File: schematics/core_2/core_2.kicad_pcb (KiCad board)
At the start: 2 copper layers, 100 x 91.1 mm, 24 parts, among them U1 74LS04, U2 74LS574, U3 74LS02, U5 74LS00

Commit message: silklayer check
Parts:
- moved kibuzzard-6911C9E9 1.10 mm to (193.5, 26.5)

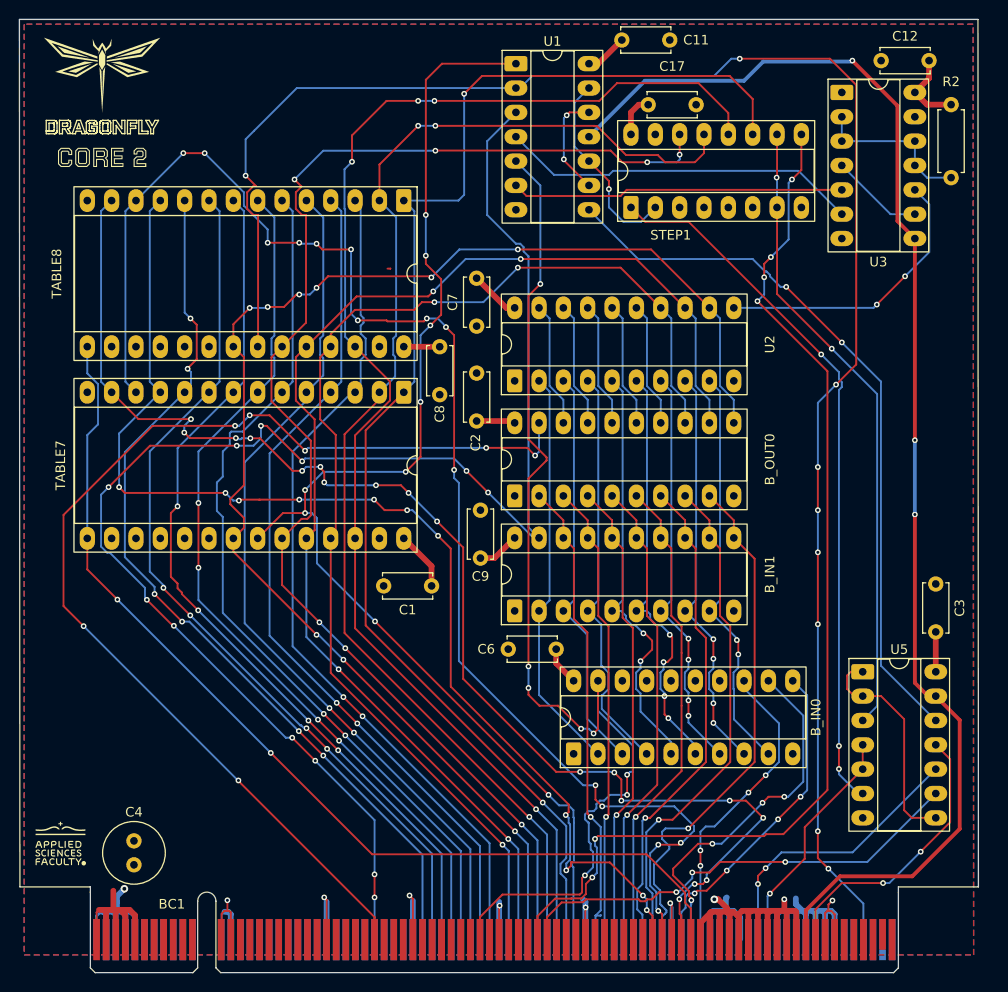
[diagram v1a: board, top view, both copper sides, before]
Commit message: fix(core2): changed vcc and gnd connection  + cooper clearence
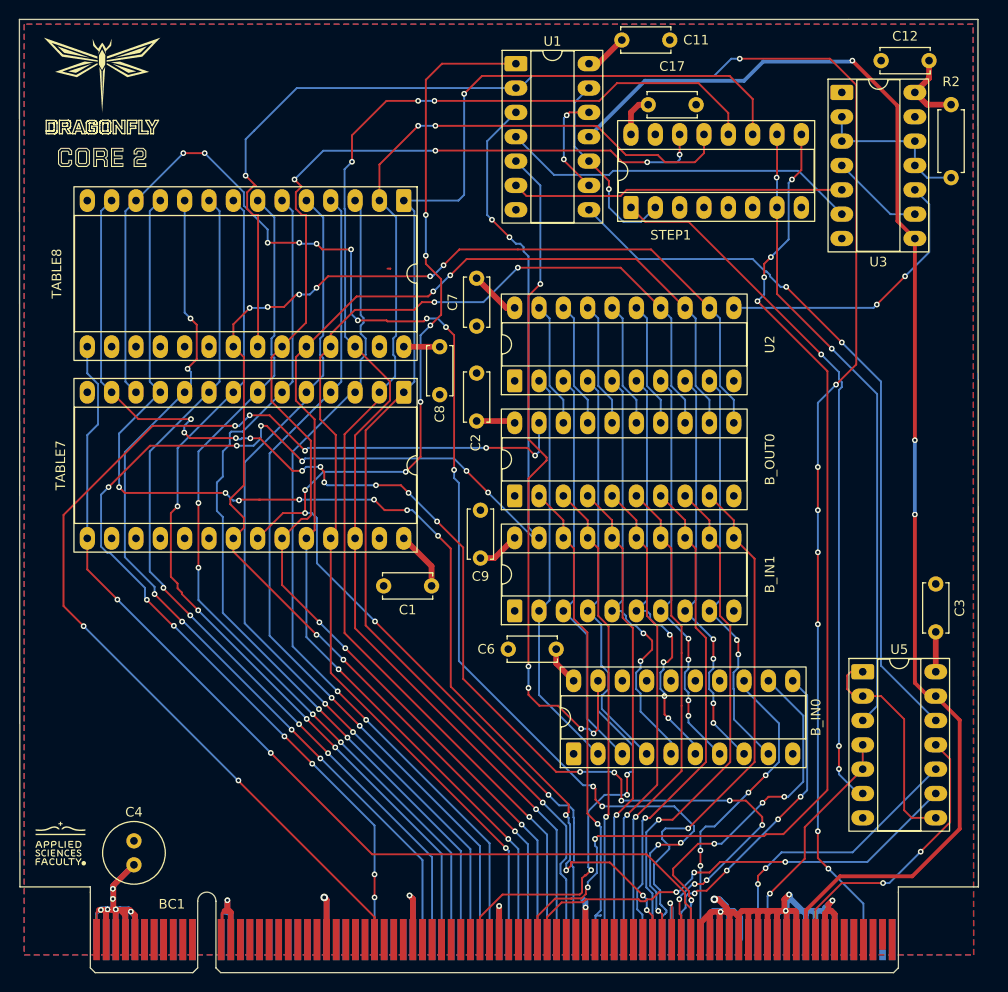
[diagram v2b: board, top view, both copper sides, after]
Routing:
- net GND: track 152.6 -> 160.5 mm, vias 9 -> 11
- net VCC: track 92.0 -> 99.6 mm, vias 1 -> 6
- net /~{UPDATE_FR}: track 115.4 -> 114.7 mm
- net /~{LOAD_FR}: track 161.5 -> 161.2 mm, vias 12 -> 14

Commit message: fix(alu, core2, interface): vcc conection some routing issues
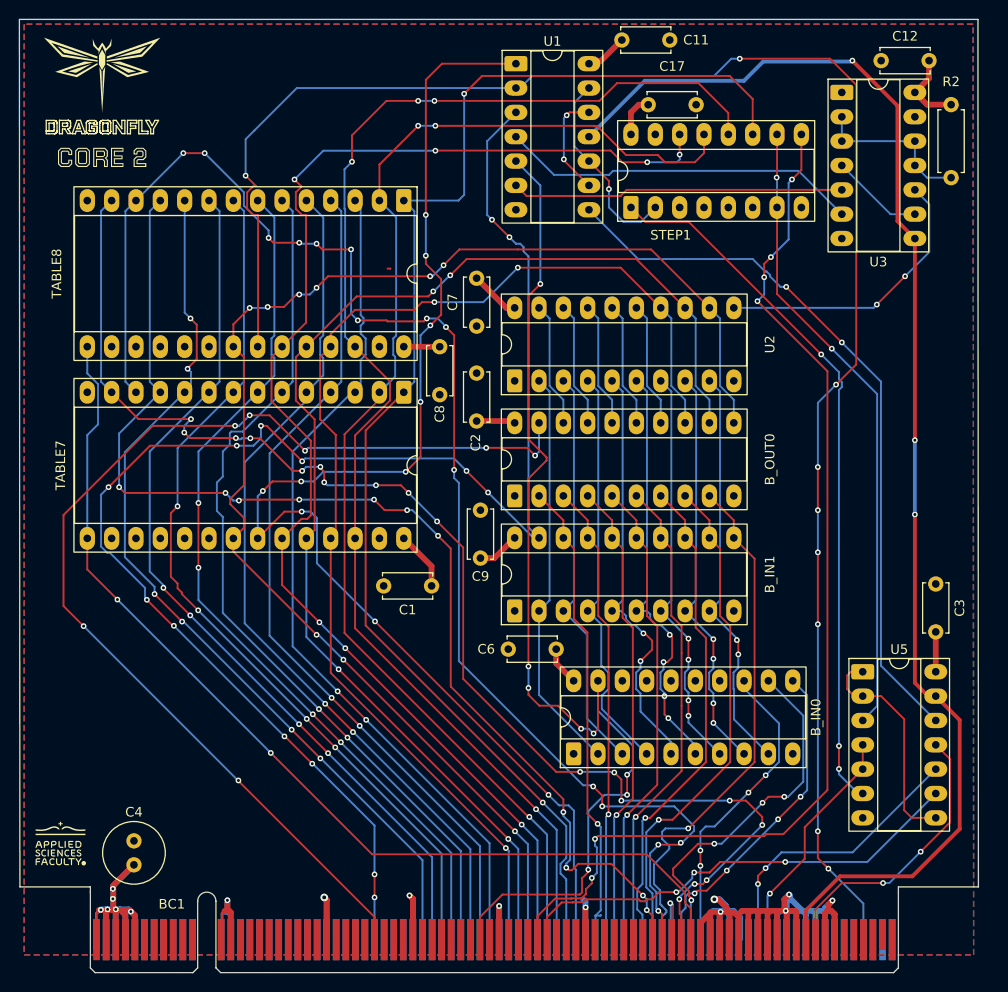
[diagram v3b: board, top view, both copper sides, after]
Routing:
- net /STATE15: track 130.3 -> 137.8 mm, vias 9 -> 10
- net /IntEnable: track 124.1 -> 123.3 mm
- net GND: track 160.5 -> 161.1 mm

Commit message: fix: removed in control pins daisy chains
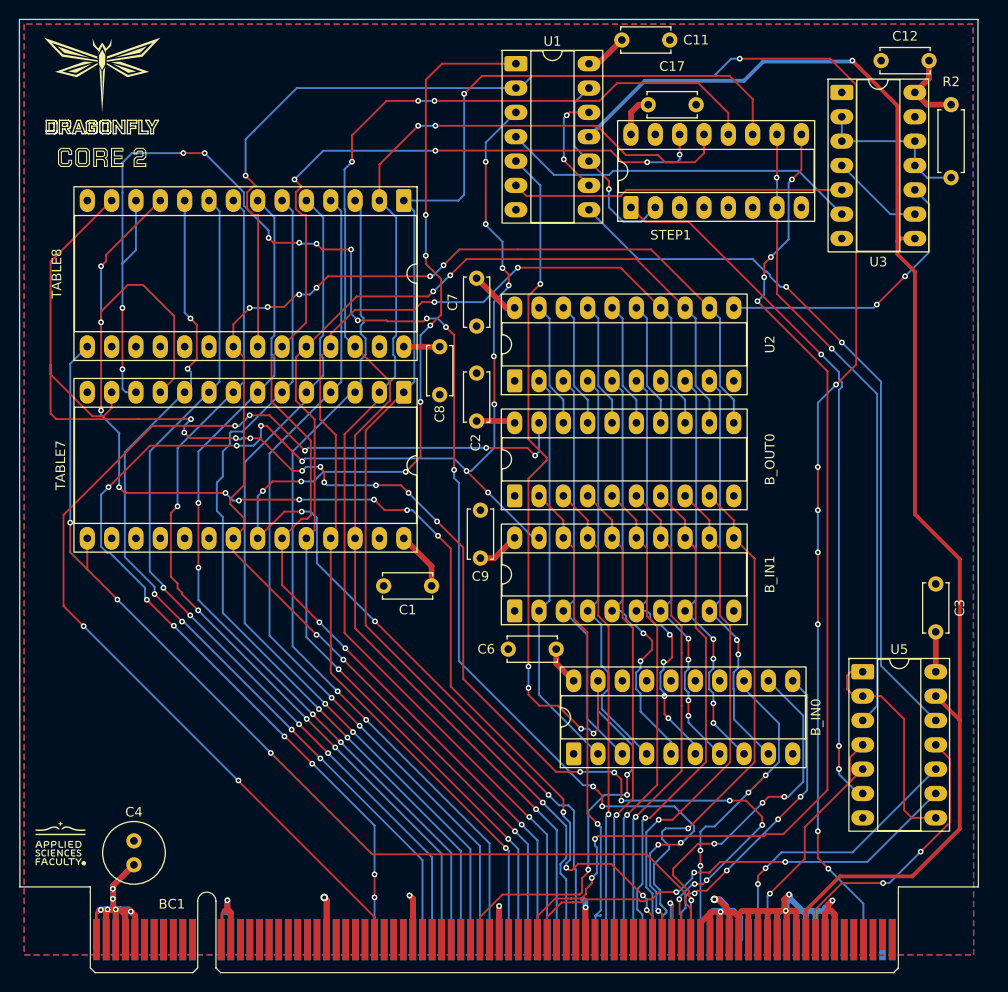
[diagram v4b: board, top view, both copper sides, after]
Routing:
- net /AddrDecrement: track 136.7 -> 157.3 mm
- net /IntEnable: track 123.3 -> 143.8 mm, vias 11 -> 14
- net /~{IntDisable}: track 151.8 -> 162.9 mm, vias 15 -> 17
- net /~{LOAD_FR}: track 161.2 -> 154.9 mm, vias 14 -> 18
- net /~CLK: track 138.6 -> 144.5 mm, vias 3 -> 1
- net /AddrIncrement: track 105.6 -> 109.4 mm, vias 2 -> 3
- net /Reset: track 24.4 -> 26.3 mm

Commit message: fix(alu, core_1_2, interface): put vcc zones on back layer
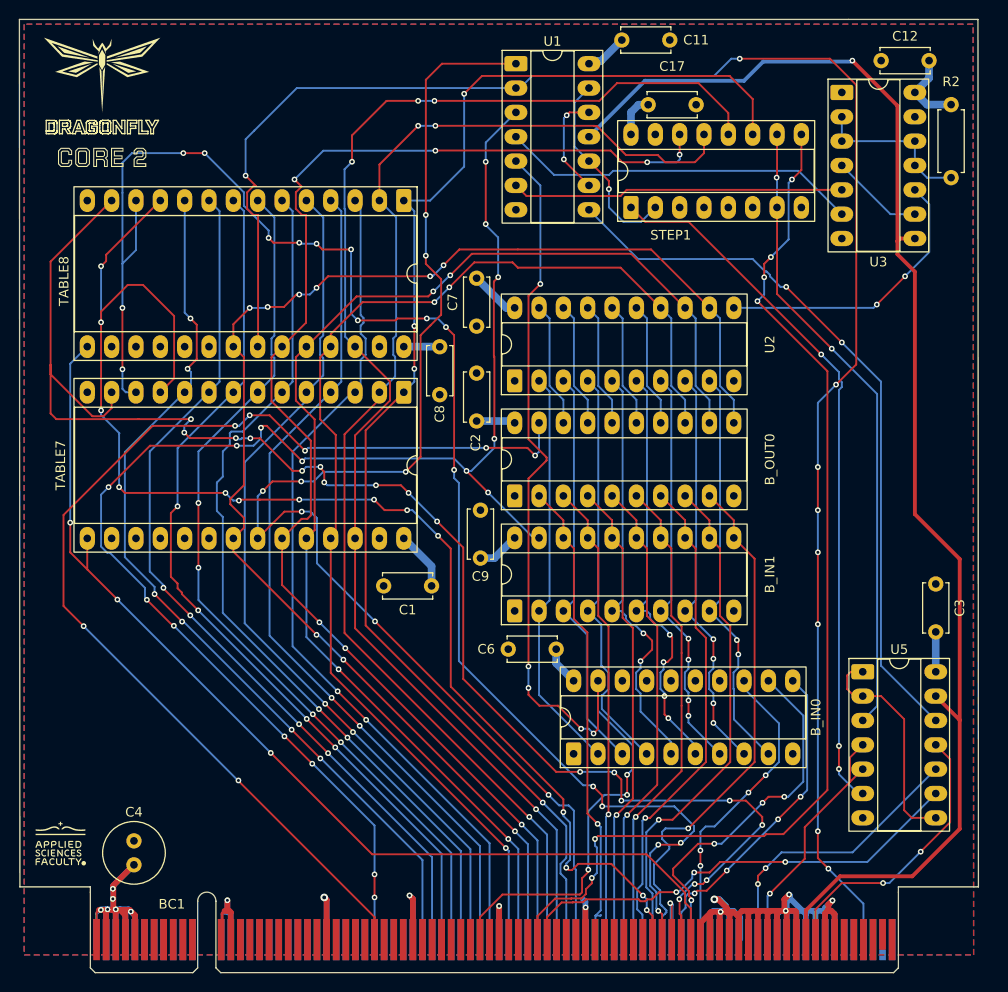
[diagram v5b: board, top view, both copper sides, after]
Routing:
- net /STATE14: track 141.5 -> 139.8 mm, vias 2 -> 4
- net /~{LOAD_FR}: track 154.9 -> 153.9 mm, vias 18 -> 16
- net /STATE15: vias 10 -> 8

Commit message: added testpoints on core 2
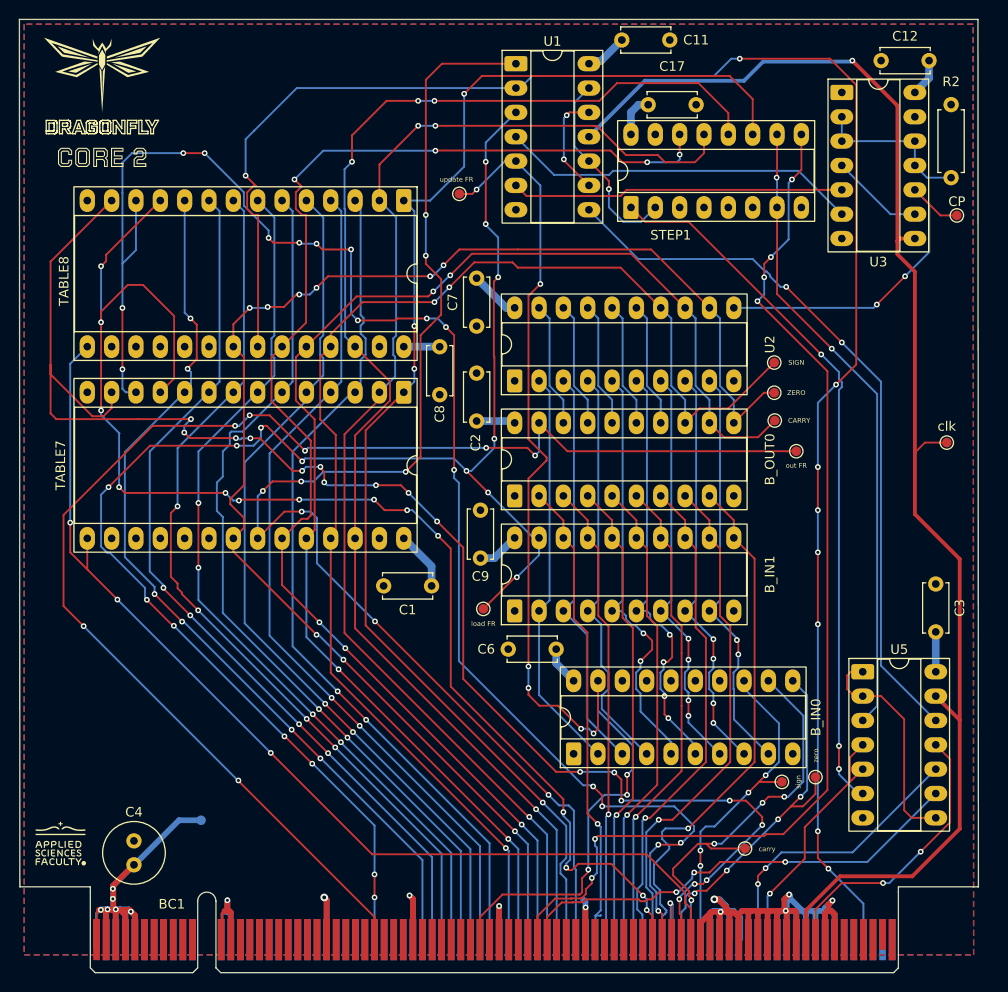
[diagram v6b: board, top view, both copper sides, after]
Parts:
- added CARRY: TestPoint, TestPoint:TestPoint_Pad_D1.0mm, F.Cu at (263.7, 54.0)
- added CP: TestPoint, TestPoint:TestPoint_Pad_D1.0mm, F.Cu at (282.7, 32.5)
- added SIGN: TestPoint, TestPoint:TestPoint_Pad_D1.0mm, F.Cu at (263.6, 47.9)
- added TP1: TestPoint, TestPoint:TestPoint_Pad_D1.0mm, B.Cu at (203.8, 95.7)
- added ZERO: TestPoint, TestPoint:TestPoint_Pad_D1.0mm, F.Cu at (263.6, 51.0)
- added carry: TestPoint, TestPoint:TestPoint_Pad_D1.0mm, F.Cu at (260.6, 98.6)
- added clk: TestPoint, TestPoint:TestPoint_Pad_D1.0mm, F.Cu at (281.6, 56.2)
- added load FR: TestPoint, TestPoint:TestPoint_Pad_D1.0mm, F.Cu at (233.3, 73.6)
- added out FR: TestPoint, TestPoint:TestPoint_Pad_D1.0mm, F.Cu at (265.9, 57.1)
- added sign: TestPoint, TestPoint:TestPoint_Pad_D1.0mm, F.Cu at (264.4, 91.7)
- added update FR: TestPoint, TestPoint:TestPoint_Pad_D1.0mm, F.Cu at (230.8, 30.3)
- added zero: TestPoint, TestPoint:TestPoint_Pad_D1.0mm, F.Cu at (267.9, 91.2)
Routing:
- net /~{OUT_FR}: track 116.8 -> 144.9 mm
- net /STATE8: track 124.8 -> 136.7 mm
- net /~{LOAD_FR}: track 153.9 -> 163.8 mm, vias 16 -> 17
- net /STATE9: track 131.6 -> 139.7 mm
- net /~{UPDATE_FR}: track 114.2 -> 121.5 mm, vias 8 -> 9
- net /STATE10: track 147.6 -> 153.1 mm
- net Net-(U2-Cp): track 29.9 -> 35.4 mm
- net /ZeroIn: track 34.0 -> 38.8 mm
- net VCC: track 99.5 -> 104.1 mm
- net /~{CarryIn}: track 37.6 -> 41.8 mm
- net /~CLK: track 144.5 -> 148.2 mm
- net /SignIn: track 32.4 -> 34.8 mm

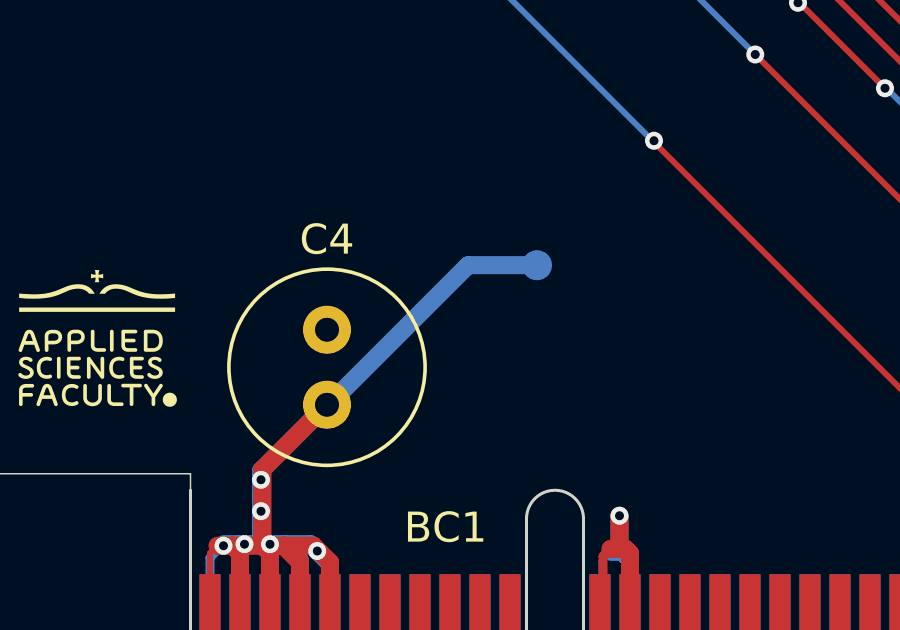
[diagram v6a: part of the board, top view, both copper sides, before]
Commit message: Add test points
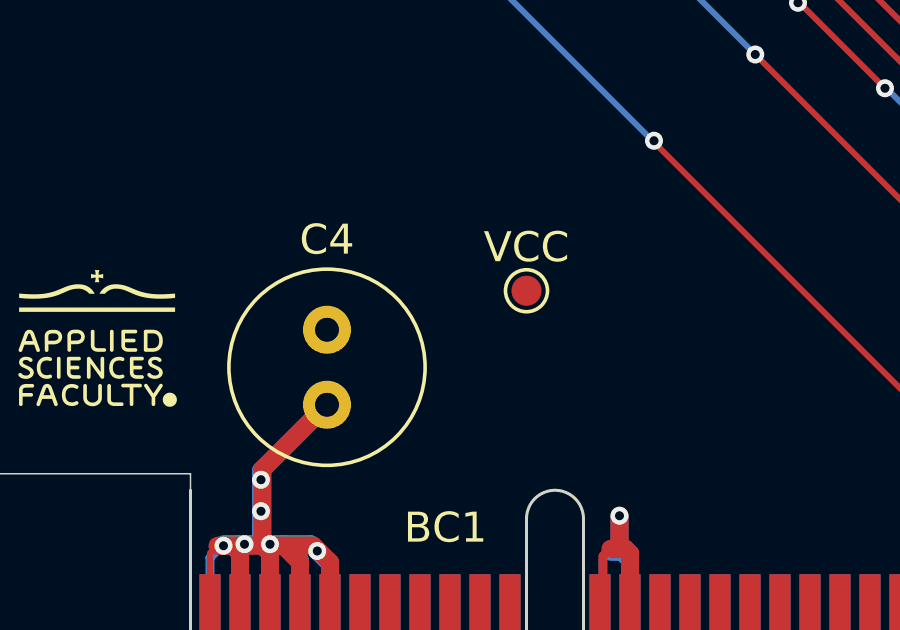
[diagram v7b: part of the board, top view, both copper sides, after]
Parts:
- VCC: renamed from TP1; moved to F.Cu
- moved VCC 0.92 mm to (203.5, 96.5), turned to 0 degrees
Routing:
- net VCC: track 104.1 -> 95.2 mm
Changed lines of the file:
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@@
 		(embedded_fonts no)
 	)
+	(footprint "TestPoint:TestPoint_Pad_D1.0mm"
+		(layer "F.Cu")
+		(at 203.5 96.5)
+		(descr "SMD pad as test Point, diameter 1.0mm")
+		(tags "test point SMD pad")
+		(property "Reference" "VCC"
+			(at 0 -1.448 0)
+			(layer "F.SilkS")
+			(effects
+				(font
+					(size 1 1)
+					(thickness 0.15)
+				)
+			)
+		)
+		(property "Value" "TestPoint"
+			(at 0 1.55 0)
+			(layer "F.Fab")
+			(effects
+				(font
+					(size 1 1)
+					(thickness 0.15)
+				)
+			)
+		)
+		(property "Datasheet" "~"
+			(at 0 0 0)
+			(unlocked yes)
+			(layer "F.Fab")
+			(hide yes)
+			(effects
+				(font
+					(size 1.27 1.27)
+					(thickness 0.15)
+				)
+			)
+		)
+		(property "Description" "test point"
+			(at 0 0 0)
+			(unlocked yes)
+			(layer "F.Fab")
+			(hide yes)
+			(effects
+				(font
+					(size 1.27 1.27)
+					(thickness 0.15)
+				)
+			)
+		)
+		(property ki_fp_filters "Pin* Test*")
+		(sheetname "/")
+		(sheetfile "core_2.kicad_sch")
+		(zone_connect 2)
+		(attr exclude_from_pos_files)
+		(fp_circle
+			(center 0 0)
+			(end 0 0.7)
+			(stroke
+				(width 0.12)
+				(type solid)
+			)
+			(fill no)
+			(layer "F.SilkS")
+		)
+		(fp_circle
+			(center 0 0)
+			(end 1 0)
+			(stroke
+				(width 0.05)
+				(type solid)
+			)
+			(fill no)
+			(layer "F.CrtYd")
+		)
+		(fp_text user "${REFERENCE}"
+			(at 0 -1.45 0)
+			(layer "F.Fab")
+			(effects
+				(font
+					(size 1 1)
+					(thickness 0.15)
+				)
+			)
+		)
+		(pad "1" smd circle
+			(at 0 0)
+			(size 1 1)
+			(layers "F.Cu" "F.Mask")
+			(net 6 "VCC")
+			(pinfunction "1")
+			(pintype "passive")
+		)
+		(embedded_fonts no)
+	)
 	(footprint "Capacitor_THT:C_Disc_D5.0mm_W2.5mm_P5.00mm"
 		(layer "F.Cu")
@@
 		(embedded_fonts no)
 	)
-	(footprint "TestPoint:TestPoint_Pad_D1.0mm"
-		(layer "B.Cu")
-		(at 203.85 95.65 180)
-		(descr "SMD pad as test Point, diameter 1.0mm")
-		(tags "test point SMD pad")
-		(property "Reference" "TP1"
-			(at 0 1.448 0)
-			(layer "B.SilkS")
-			(effects
-				(font
-					(size 1 1)
-					(thickness 0.15)
-				)
-				(justify mirror)
-			)
-		)
-		(property "Value" "TestPoint"
-			(at 0 -1.55 0)
-			(layer "B.Fab")
-			(effects
-				(font
-					(size 1 1)
-					(thickness 0.15)
-				)
-				(justify mirror)
-			)
-		)
-		(property "Datasheet" "~"
-			(at 0 0 0)
-			(unlocked yes)
-			(layer "B.Fab")
-			(hide yes)
-			(effects
-				(font
-					(size 1.27 1.27)
-					(thickness 0.15)
-				)
-				(justify mirror)
-			)
-		)
-		(property "Description" "test point"
-			(at 0 0 0)
-			(unlocked yes)
-			(layer "B.Fab")
-			(hide yes)
-			(effects
-				(font
-					(size 1.27 1.27)
-					(thickness 0.15)
-				)
-				(justify mirror)
-			)
-		)
-		(property ki_fp_filters "Pin* Test*")
-		(sheetname "/")
-		(sheetfile "core_2.kicad_sch")
-		(attr exclude_from_pos_files)
-		(fp_circle
-			(center 0 0)
-			(end 0 -0.7)
-			(stroke
-				(width 0.12)
-				(type solid)
-			)
-			(fill no)
-			(layer "B.SilkS")
-		)
-		(fp_circle
-			(center 0 0)
-			(end 1 0)
-			(stroke
-				(width 0.05)
-				(type solid)
-			)
-			(fill no)
-			(layer "B.CrtYd")
-		)
-		(fp_text user "${REFERENCE}"
-			(at 0 1.45 0)
-			(layer "B.Fab")
-			(effects
-				(font
-					(size 1 1)
-					(thickness 0.15)
-				)
-				(justify mirror)
-			)
-		)
-		(pad "1" smd circle
-			(at 0 0 180)
-			(size 1 1)
-			(layers "B.Cu" "B.Mask")
-			(net 6 "VCC")
-			(pinfunction "1")
-			(pintype "passive")
-		)
-		(embedded_fonts no)
-	)
 	(gr_poly
 		(pts
@@
 	)
 	(segment
-		(start 196.9 100.3)
-		(end 201.55 95.65)
-		(width 0.6)
-		(layer "B.Cu")
-		(net 6)
-	)
-	(segment
 		(start 194.65 102.8)
 		(end 194.65 102.5)
@@
 		(layer "B.Cu")
 		(net 6)
-	)
-	(segment
-		(start 201.55 95.65)
-		(end 203.85 95.65)
-		(width 0.6)
-		(layer "B.Cu")
-		(net 6)
